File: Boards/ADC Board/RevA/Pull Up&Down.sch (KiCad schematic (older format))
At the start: 4 parts

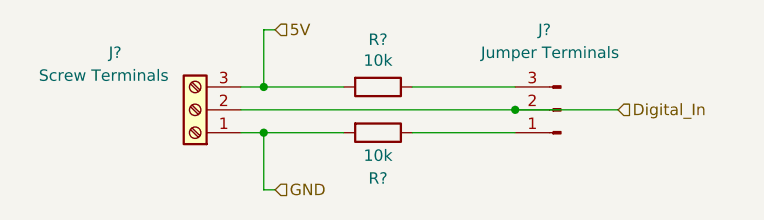
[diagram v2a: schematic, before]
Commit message: Connected power regulator to ADC and micro boards. Added no connects to headers on ADC board. Preformed some footprinting operations on ADC board.
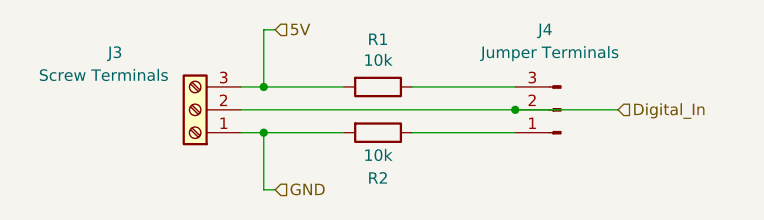
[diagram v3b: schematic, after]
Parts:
- gave numbers to parts that had none: 4
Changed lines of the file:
@@
 $EndDescr
 $Comp
-L Connector:Screw_Terminal_01x03 J?
+L Connector:Screw_Terminal_01x03 J3
 U 1 1 615FC6ED
 P 2150 1200
-AR Path="/61593BCA/615FC6ED" Ref="J?"  Part="1"
+AR Path="/61593BCA/615FC6ED" Ref="J3"  Part="1"
 AR Path="/61640BD1/615FC6ED" Ref="J?"  Part="1"
 AR Path="/61641449/615FC6ED" Ref="J?"  Part="1"
 AR Path="/6164144B/615FC6ED" Ref="J?"  Part="1"
-AR Path="/616422A2/615FC6ED" Ref="J?"  Part="1"
-AR Path="/616423D2/615FC6ED" Ref="J?"  Part="1"
-AR Path="/616425FE/615FC6ED" Ref="J?"  Part="1"
-F 0 "J?" H 2500 950 50  0000 C CNN
+AR Path="/616422A2/615FC6ED" Ref="J5"  Part="1"
+AR Path="/616423D2/615FC6ED" Ref="J7"  Part="1"
+AR Path="/616425FE/615FC6ED" Ref="J9"  Part="1"
+F 0 "J3" H 2500 950 50  0000 C CNN
 F 1 "Screw Terminals" H 2550 1050 50  0000 C CNN
 F 2 "" H 2150 1200 50  0001 C CNN
@@
 5V
 $Comp
-L Device:R R?
+L Device:R R1
 U 1 1 616034B0
 P 2950 1100
-AR Path="/61593BCA/616034B0" Ref="R?"  Part="1"
+AR Path="/61593BCA/616034B0" Ref="R1"  Part="1"
 AR Path="/61640BD1/616034B0" Ref="R?"  Part="1"
 AR Path="/61641449/616034B0" Ref="R?"  Part="1"
 AR Path="/6164144B/616034B0" Ref="R?"  Part="1"
-AR Path="/616422A2/616034B0" Ref="R?"  Part="1"
-AR Path="/616423D2/616034B0" Ref="R?"  Part="1"
-AR Path="/616425FE/616034B0" Ref="R?"  Part="1"
-F 0 "R?" V 2743 1100 50  0000 C CNN
+AR Path="/616422A2/616034B0" Ref="R3"  Part="1"
+AR Path="/616423D2/616034B0" Ref="R5"  Part="1"
+AR Path="/616425FE/616034B0" Ref="R7"  Part="1"
+F 0 "R1" V 2743 1100 50  0000 C CNN
 F 1 "10k" V 2834 1100 50  0000 C CNN
 F 2 "" V 2880 1100 50  0001 C CNN
@@
 $EndComp
 $Comp
-L Device:R R?
+L Device:R R2
 U 1 1 61604CD1
 P 2950 1300
-AR Path="/61593BCA/61604CD1" Ref="R?"  Part="1"
+AR Path="/61593BCA/61604CD1" Ref="R2"  Part="1"
 AR Path="/61640BD1/61604CD1" Ref="R?"  Part="1"
 AR Path="/61641449/61604CD1" Ref="R?"  Part="1"
 AR Path="/6164144B/61604CD1" Ref="R?"  Part="1"
-AR Path="/616422A2/61604CD1" Ref="R?"  Part="1"
-AR Path="/616423D2/61604CD1" Ref="R?"  Part="1"
-AR Path="/616425FE/61604CD1" Ref="R?"  Part="1"
-F 0 "R?" V 3150 1300 50  0000 C CNN
+AR Path="/616422A2/61604CD1" Ref="R4"  Part="1"
+AR Path="/616423D2/61604CD1" Ref="R6"  Part="1"
+AR Path="/616425FE/61604CD1" Ref="R8"  Part="1"
+F 0 "R2" V 3150 1300 50  0000 C CNN
 F 1 "10k" V 3050 1300 50  0000 C CNN
 F 2 "" V 2880 1300 50  0001 C CNN
@@
 	2800 1300 2450 1300
 $Comp
-L Connector:Conn_01x03_Male J?
+L Connector:Conn_01x03_Male J4
 U 1 1 61613676
 P 3750 1200
-AR Path="/61593BCA/61613676" Ref="J?"  Part="1"
+AR Path="/61593BCA/61613676" Ref="J4"  Part="1"
 AR Path="/61640BD1/61613676" Ref="J?"  Part="1"
 AR Path="/61641449/61613676" Ref="J?"  Part="1"
 AR Path="/6164144B/61613676" Ref="J?"  Part="1"
-AR Path="/616422A2/61613676" Ref="J?"  Part="1"
-AR Path="/616423D2/61613676" Ref="J?"  Part="1"
-AR Path="/616425FE/61613676" Ref="J?"  Part="1"
-F 0 "J?" H 3850 850 50  0000 R CNN
+AR Path="/616422A2/61613676" Ref="J6"  Part="1"
+AR Path="/616423D2/61613676" Ref="J8"  Part="1"
+AR Path="/616425FE/61613676" Ref="J10"  Part="1"
+F 0 "J4" H 3850 850 50  0000 R CNN
 F 1 "Jumper Terminals" H 4100 950 50  0000 R CNN
 F 2 "" H 3750 1200 50  0001 C CNN

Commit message: Fixed regulator nonsense on ADC board. Rules checked both ADC and micro boards. Fixed interconnect on ADC board.
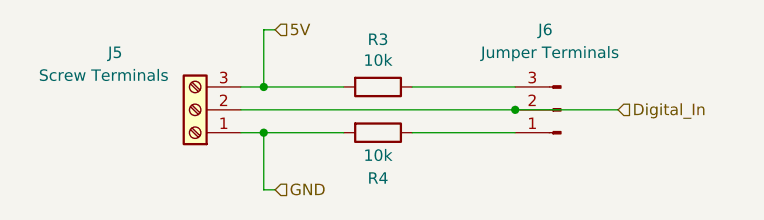
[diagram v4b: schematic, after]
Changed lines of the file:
@@
 $Descr A4 11693 8268
 encoding utf-8
-Sheet 2 11
+Sheet 3 11
 Title ""
 Date ""
@@
 AR Path="/616423D2/615FC6ED" Ref="J7"  Part="1"
 AR Path="/616425FE/615FC6ED" Ref="J9"  Part="1"
-F 0 "J3" H 2500 950 50  0000 C CNN
+F 0 "J5" H 2500 950 50  0000 C CNN
 F 1 "Screw Terminals" H 2550 1050 50  0000 C CNN
 F 2 "" H 2150 1200 50  0001 C CNN
@@
 AR Path="/616423D2/616034B0" Ref="R5"  Part="1"
 AR Path="/616425FE/616034B0" Ref="R7"  Part="1"
-F 0 "R1" V 2743 1100 50  0000 C CNN
+F 0 "R3" V 2743 1100 50  0000 C CNN
 F 1 "10k" V 2834 1100 50  0000 C CNN
 F 2 "" V 2880 1100 50  0001 C CNN
@@
 AR Path="/616423D2/61604CD1" Ref="R6"  Part="1"
 AR Path="/616425FE/61604CD1" Ref="R8"  Part="1"
-F 0 "R2" V 3150 1300 50  0000 C CNN
+F 0 "R4" V 3150 1300 50  0000 C CNN
 F 1 "10k" V 3050 1300 50  0000 C CNN
 F 2 "" V 2880 1300 50  0001 C CNN
@@
 AR Path="/616423D2/61613676" Ref="J8"  Part="1"
 AR Path="/616425FE/61613676" Ref="J10"  Part="1"
-F 0 "J4" H 3850 850 50  0000 R CNN
+F 0 "J6" H 3850 850 50  0000 R CNN
 F 1 "Jumper Terminals" H 4100 950 50  0000 R CNN
 F 2 "" H 3750 1200 50  0001 C CNN

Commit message: Began PCB layout for ADC board. Fixed annotations for ADC and micro boards.
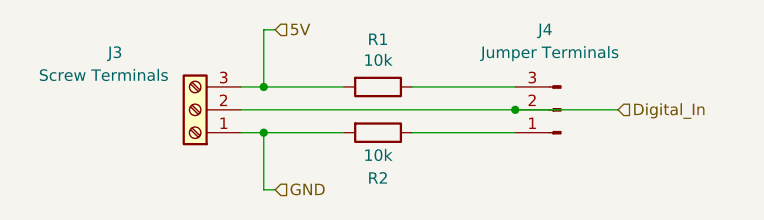
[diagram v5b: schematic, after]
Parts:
- R1, R2: footprint (none) -> Resistor_SMD:R_0603_1608Metric
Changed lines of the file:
@@
 $Descr A4 11693 8268
 encoding utf-8
-Sheet 3 11
+Sheet 2 11
 Title ""
 Date ""
@@
 AR Path="/616423D2/615FC6ED" Ref="J7"  Part="1"
 AR Path="/616425FE/615FC6ED" Ref="J9"  Part="1"
-F 0 "J5" H 2500 950 50  0000 C CNN
+F 0 "J3" H 2500 950 50  0000 C CNN
 F 1 "Screw Terminals" H 2550 1050 50  0000 C CNN
 F 2 "" H 2150 1200 50  0001 C CNN
@@
 AR Path="/616423D2/616034B0" Ref="R5"  Part="1"
 AR Path="/616425FE/616034B0" Ref="R7"  Part="1"
-F 0 "R3" V 2743 1100 50  0000 C CNN
+F 0 "R1" V 2743 1100 50  0000 C CNN
 F 1 "10k" V 2834 1100 50  0000 C CNN
-F 2 "" V 2880 1100 50  0001 C CNN
+F 2 "Resistor_SMD:R_0603_1608Metric" V 2880 1100 50  0001 C CNN
 F 3 "~" H 2950 1100 50  0001 C CNN
 	1    2950 1100
@@
 AR Path="/616423D2/61604CD1" Ref="R6"  Part="1"
 AR Path="/616425FE/61604CD1" Ref="R8"  Part="1"
-F 0 "R4" V 3150 1300 50  0000 C CNN
+F 0 "R2" V 3150 1300 50  0000 C CNN
 F 1 "10k" V 3050 1300 50  0000 C CNN
-F 2 "" V 2880 1300 50  0001 C CNN
+F 2 "Resistor_SMD:R_0603_1608Metric" V 2880 1300 50  0001 C CNN
 F 3 "~" H 2950 1300 50  0001 C CNN
 	1    2950 1300
@@
 AR Path="/616423D2/61613676" Ref="J8"  Part="1"
 AR Path="/616425FE/61613676" Ref="J10"  Part="1"
-F 0 "J6" H 3850 850 50  0000 R CNN
+F 0 "J4" H 3850 850 50  0000 R CNN
 F 1 "Jumper Terminals" H 4100 950 50  0000 R CNN
 F 2 "" H 3750 1200 50  0001 C CNN

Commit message: Completed footprint associations for ADC board. Generated netlist for ADC board. Started PCB design for ADC board.
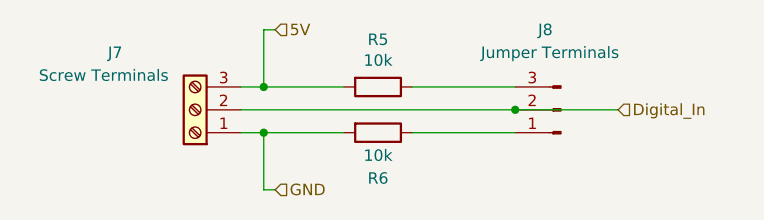
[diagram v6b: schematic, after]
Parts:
- J3, J4: footprint (none) -> Connector_PinHeader_2.54mm:PinHeader_1x03_P2.54mm_Vertical
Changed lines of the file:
@@
 $Descr A4 11693 8268
 encoding utf-8
-Sheet 2 11
+Sheet 4 11
 Title ""
 Date ""
@@
 AR Path="/616423D2/615FC6ED" Ref="J7"  Part="1"
 AR Path="/616425FE/615FC6ED" Ref="J9"  Part="1"
-F 0 "J3" H 2500 950 50  0000 C CNN
+F 0 "J7" H 2500 950 50  0000 C CNN
 F 1 "Screw Terminals" H 2550 1050 50  0000 C CNN
-F 2 "" H 2150 1200 50  0001 C CNN
+F 2 "Connector_PinHeader_2.54mm:PinHeader_1x03_P2.54mm_Vertical" H 2150 1200 50  0001 C CNN
 F 3 "~" H 2150 1200 50  0001 C CNN
 	1    2150 1200
@@
 AR Path="/616423D2/616034B0" Ref="R5"  Part="1"
 AR Path="/616425FE/616034B0" Ref="R7"  Part="1"
-F 0 "R1" V 2743 1100 50  0000 C CNN
+F 0 "R5" V 2743 1100 50  0000 C CNN
 F 1 "10k" V 2834 1100 50  0000 C CNN
 F 2 "Resistor_SMD:R_0603_1608Metric" V 2880 1100 50  0001 C CNN
@@
 AR Path="/616423D2/61604CD1" Ref="R6"  Part="1"
 AR Path="/616425FE/61604CD1" Ref="R8"  Part="1"
-F 0 "R2" V 3150 1300 50  0000 C CNN
+F 0 "R6" V 3150 1300 50  0000 C CNN
 F 1 "10k" V 3050 1300 50  0000 C CNN
 F 2 "Resistor_SMD:R_0603_1608Metric" V 2880 1300 50  0001 C CNN
@@
 AR Path="/616423D2/61613676" Ref="J8"  Part="1"
 AR Path="/616425FE/61613676" Ref="J10"  Part="1"
-F 0 "J4" H 3850 850 50  0000 R CNN
+F 0 "J8" H 3850 850 50  0000 R CNN
 F 1 "Jumper Terminals" H 4100 950 50  0000 R CNN
-F 2 "" H 3750 1200 50  0001 C CNN
+F 2 "Connector_PinHeader_2.54mm:PinHeader_1x03_P2.54mm_Vertical" H 3750 1200 50  0001 C CNN
 F 3 "~" H 3750 1200 50  0001 C CNN
 	1    3750 1200
